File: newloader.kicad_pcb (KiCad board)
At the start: 4 copper layers, 103.3 x 55.8 mm, 44 parts, among them J1 CES, J2 BUTTONS, U1 LTV-847S, U2 LTV-847S, U3 LTV-847S, U4 LTV-847S, U5 LTV-847S

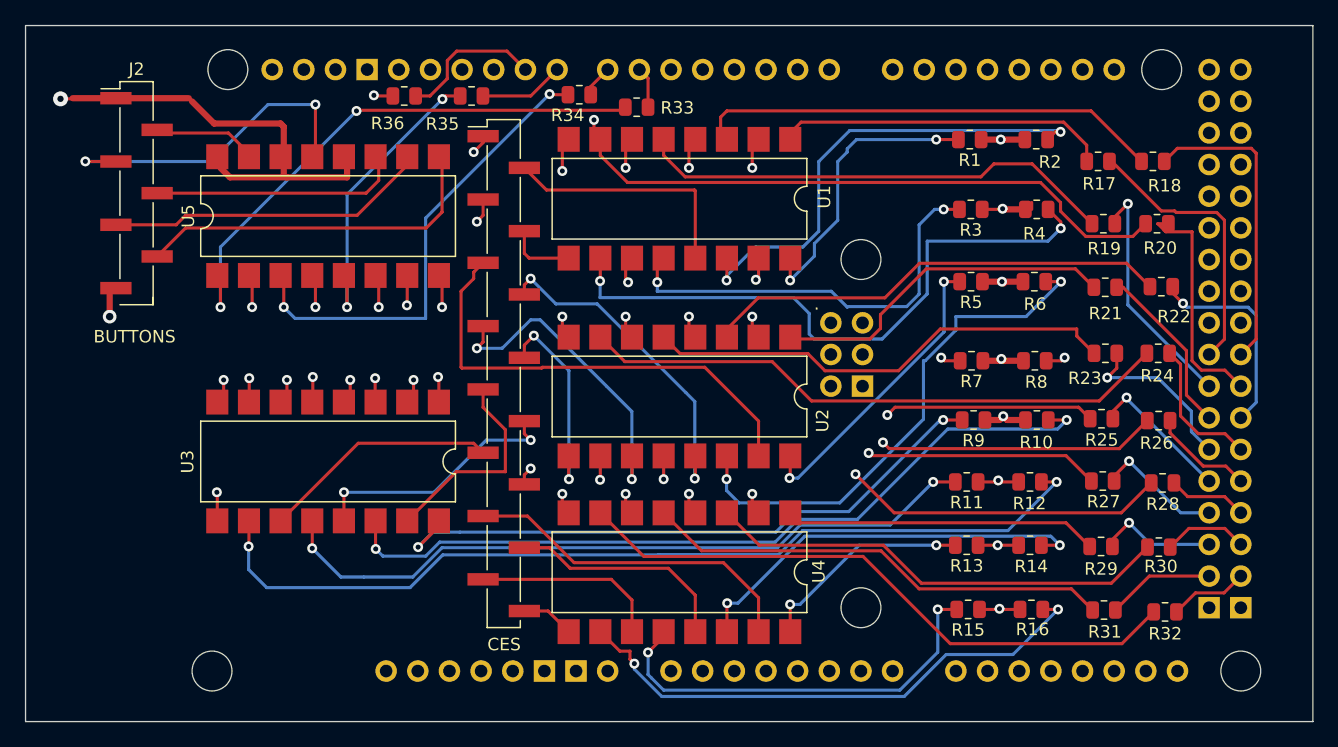
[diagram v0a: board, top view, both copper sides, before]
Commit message: V3 for easier parts purchase of 16 pin header
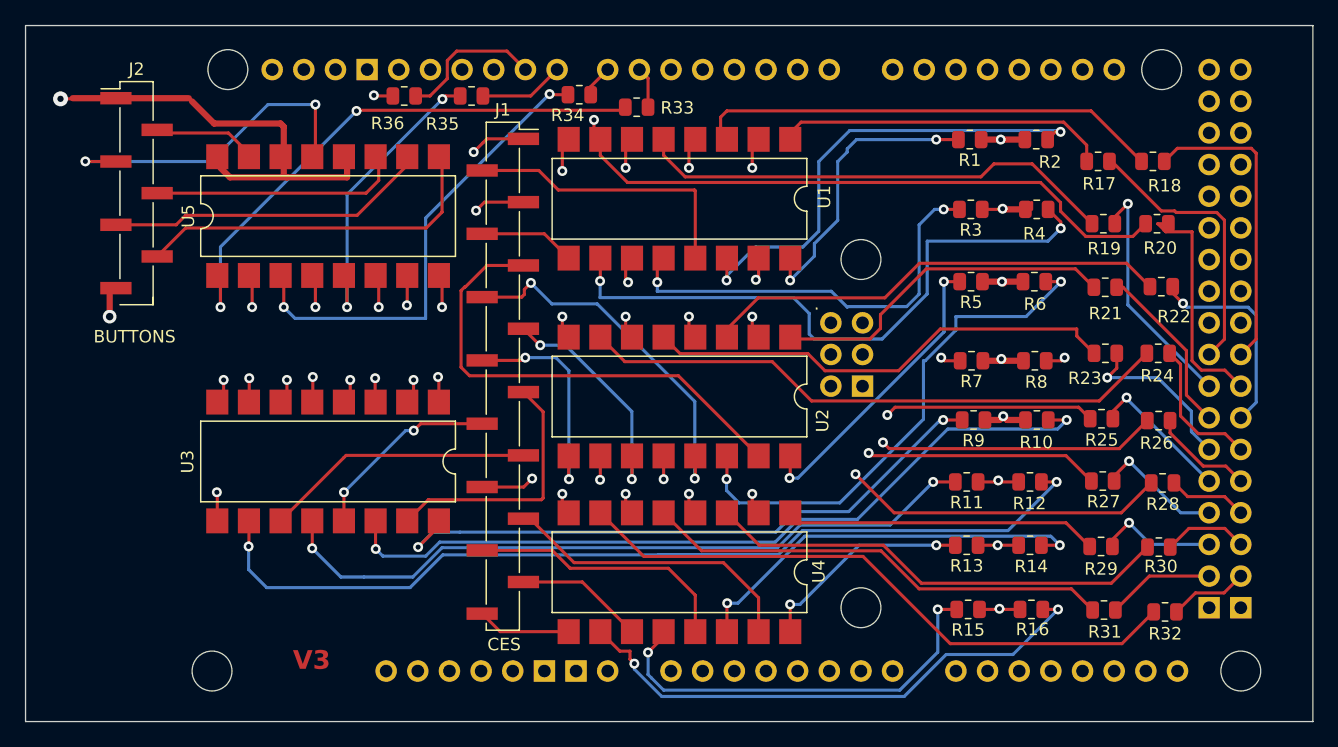
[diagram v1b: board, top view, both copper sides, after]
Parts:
- J1: footprint Connector_PinHeader_2.54mm:PinHeader_1x16_P2.54mm_Vertical_SMD_Pin1Left -> Connector_PinHeader_2.54mm:PinHeader_1x16_P2.54mm_Vertical_SMD_Pin1Right
- moved J1 0.22 mm to (139.5, 90.9)
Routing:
- net Net-(J1-Pin_7): track 25.7 -> 18.8 mm
- net Net-(J1-Pin_10): track 20.7 -> 15.7 mm
- net Net-(J1-Pin_15): track 15.2 -> 10.4 mm
- net Net-(J1-Pin_9): track 16.9 -> 20.8 mm
- net Net-(J1-Pin_13): track 27.5 -> 24.0 mm
- net Net-(J1-Pin_2): track 19.9 -> 23.2 mm
- net Net-(J1-Pin_16): track 4.24 -> 7.54 mm
- net Net-(J1-Pin_14): track 18.2 -> 21.5 mm
- net Net-(J1-Pin_12): track 29.8 -> 33.0 mm
- net Net-(J1-Pin_6): track 26.8 -> 29.7 mm
- net Net-(J1-Pin_1): track 34.0 -> 36.9 mm
- net Net-(J1-Pin_3): track 19.5 -> 22.1 mm
- net Net-(J1-Pin_11): track 19.1 -> 21.7 mm
- net Net-(J1-Pin_4): track 5.49 -> 7.75 mm
- net Net-(J1-Pin_8): track 16.7 -> 18.1 mm
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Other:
- board text added: "V3"

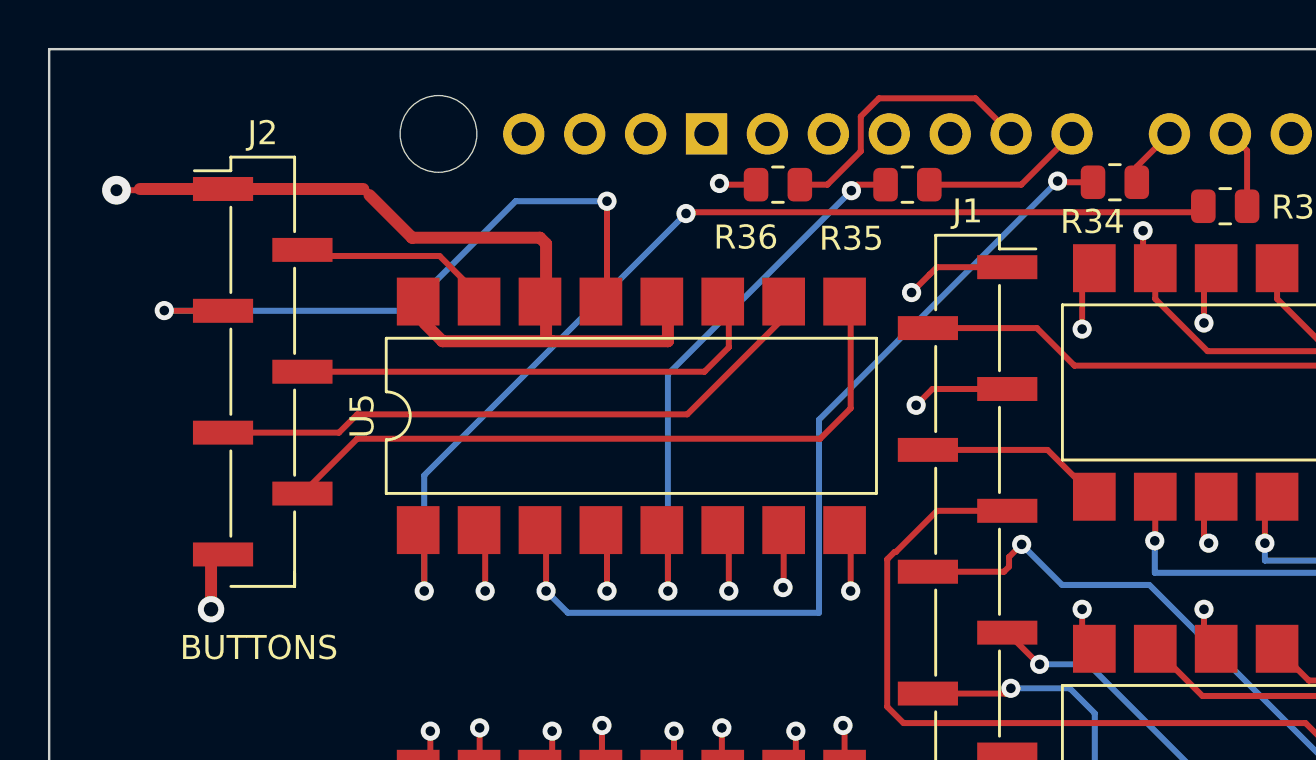
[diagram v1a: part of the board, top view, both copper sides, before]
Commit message: V4 with alternate wiring to 1130
Prior wiring method allowed bounce to show up as multiple button presses. New method solves that issue.
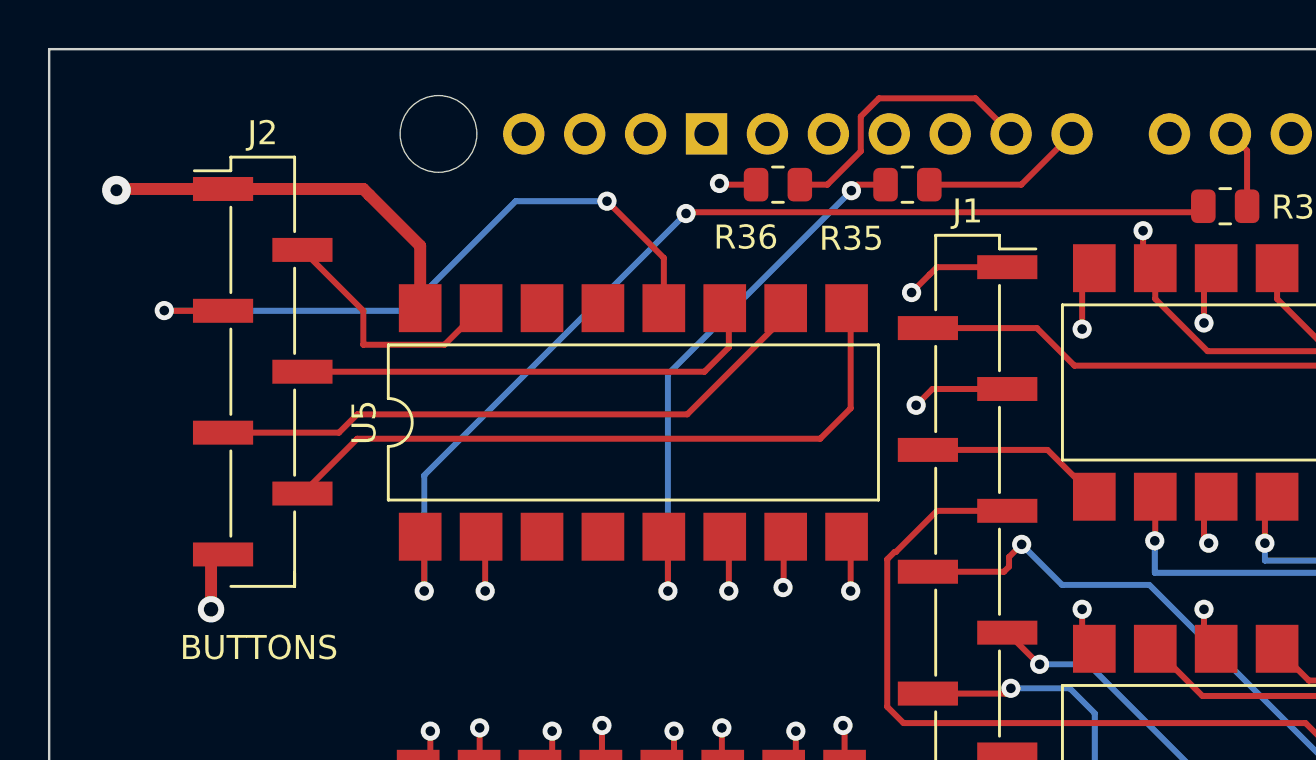
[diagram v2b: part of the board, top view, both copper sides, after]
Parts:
- removed R34: 470, Resistor_SMD:R_0805_2012Metric
- moved U5 0.29 mm to (125.6, 78.3)
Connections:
- A1 pad D7: Net-(A1-PadD7) -> unconnected-(A1-PadD7)
- U5 pad 12: +12V -> Net-(J2-Pin_3)
- U5 pad 13: Net-(J2-Pin_3) -> (no net)
- U5 pad 14: +12V -> (no net)
- U5 pad 3: Net-(R34-Pad2) -> (no net)
- U5 pad 4: GND -> (no net)
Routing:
- net Net-(R34-Pad2): track 37.9 -> 0.00 mm, vias 2 -> 0
- net +12V: track 297.9 -> 279.0 mm
- net Net-(A1-PadD7): track 2.58 -> 0.00 mm
- net GND: track 41.3 -> 38.8 mm, vias 21 -> 20
- net Net-(J2-Pin_2): track 8.51 -> 10.5 mm
- net Net-(J2-Pin_3): track 27.0 -> 28.3 mm
